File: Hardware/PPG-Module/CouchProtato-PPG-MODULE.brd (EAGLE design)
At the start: 160 x 100 mm, 0 parts

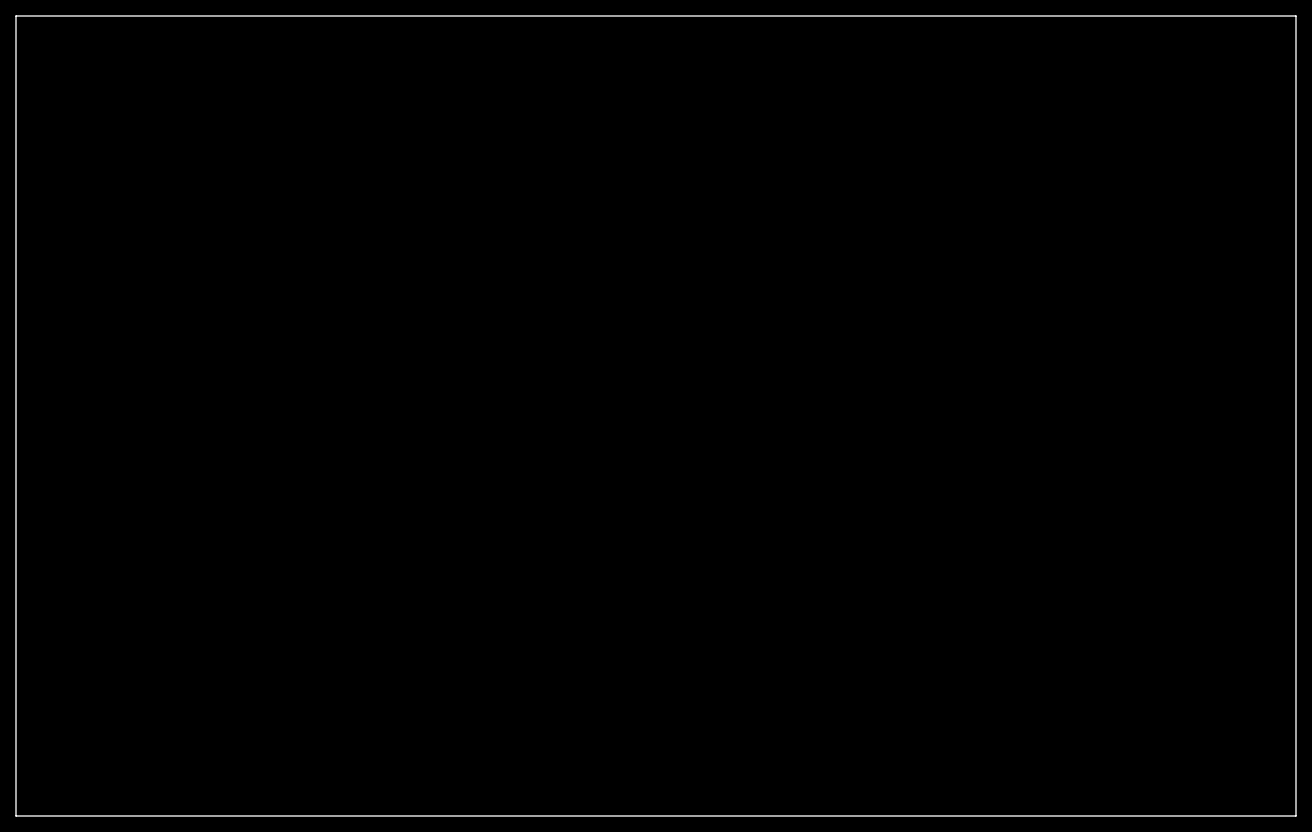
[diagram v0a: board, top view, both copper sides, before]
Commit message: Added ppg board and schematic
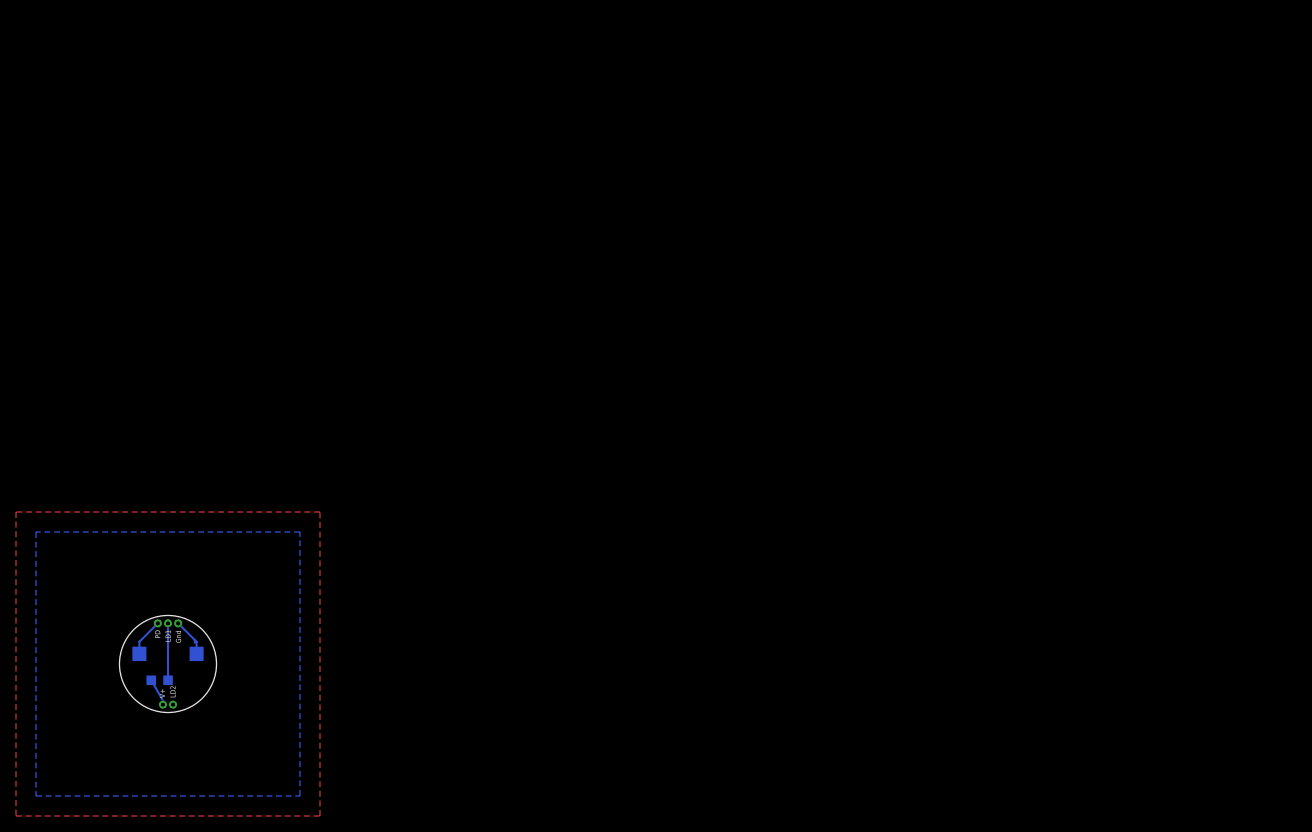
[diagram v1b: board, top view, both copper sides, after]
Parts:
- added LED: (no value), LinnesLab-LED:LED-0805
- added PD: (no value), LinnesLab-Sensors:2-SMD.GULLWING
- added U$3: (no value), LinnesLab-Connectors:PPG.MODULE.2
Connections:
- new net GND: PD.+, U$3.GND
- new net LED.C: LED.C, U$3.LD1
- new net PD.C: PD.-, U$3.PD
- new net V+: LED.A, U$3.V+
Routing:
- net LED.C: track 0.00 -> 7.11 mm
- net GND: track 0.00 -> 5.10 mm
- net PD.C: track 0.00 -> 4.77 mm
- net V+: track 0.00 -> 3.71 mm
- added copper zone on layer 1, net 3.3V
- added copper zone on layer 16, net GND
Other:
- board outline removed
